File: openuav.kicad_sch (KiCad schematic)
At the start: 69 parts, among them J1 Conn_01x01, J10 Conn_01x01, J11 Conn_01x01, J12 Conn_01x01, J13 Conn_01x01, J14 Conn_01x01, J15 Conn_01x01, J16 Conn_01x01, J17 Conn_01x01, J18 Conn_01x01, J19 Conn_01x01, J2 Conn_01x01, J20 Conn_01x01, J21 Conn_01x01, J22 Conn_01x01, J23 Conn_01x01, J24 Conn_01x01, J25 Conn_01x01, J26 Conn_01x01, J27 Conn_01x01, J28 Conn_01x01, J29 Conn_01x01, J3 Conn_01x01, J30 Conn_01x01, J31 Conn_01x01, J4 Conn_01x01, J5 Conn_01x01, J6 Conn_01x01, J7 Conn_01x01, J8 Conn_01x01, J9 Conn_01x01, J99 USB_C_Receptacle_USB2.0, SW1 SW_Push, U1 STM32G474CETx, U2 BMI270, U3 BMP280, U5 TPS54202DDC, U6 W25N01GVZEIG, U7 XC6206P332MR

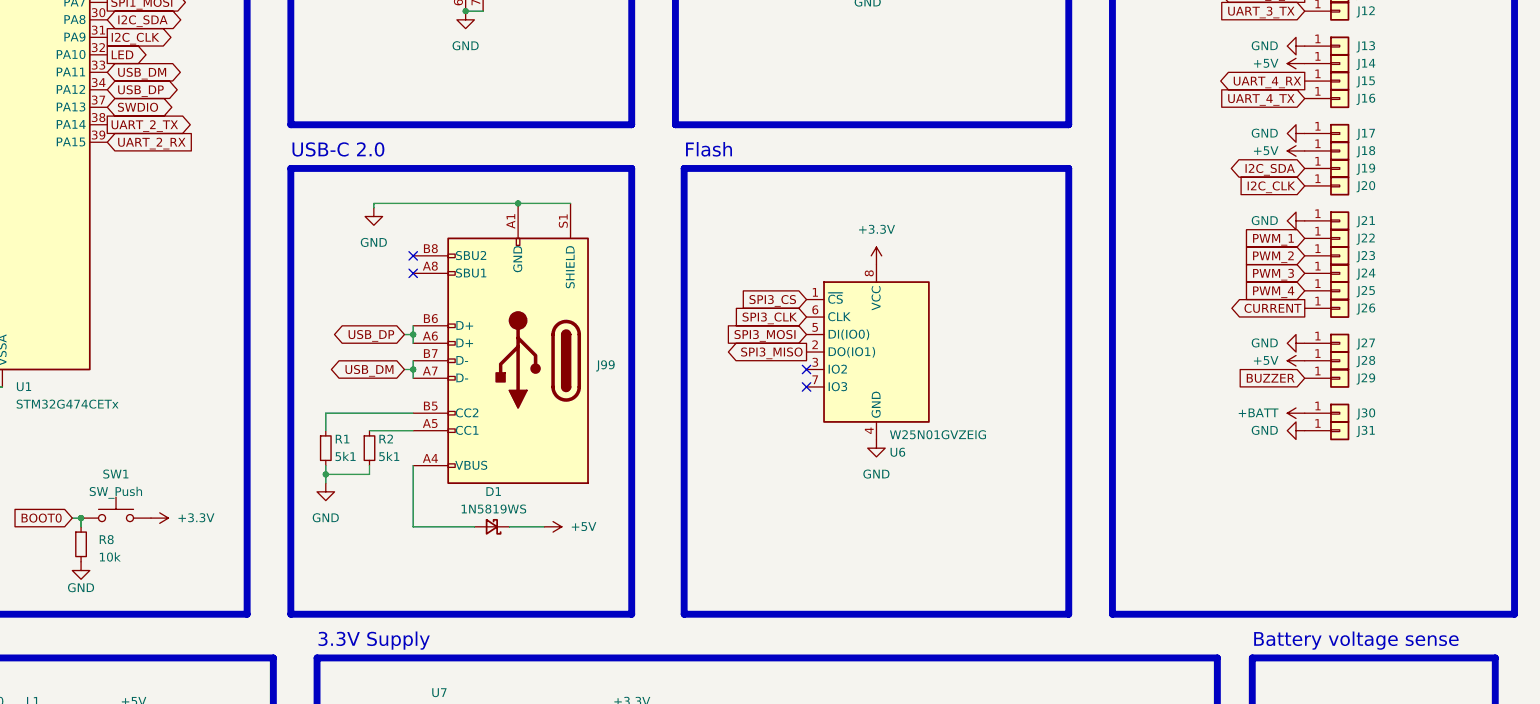
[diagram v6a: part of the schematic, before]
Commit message: continues work on G474 layout TODO: the pin space is 2.5mm not 2.54mm
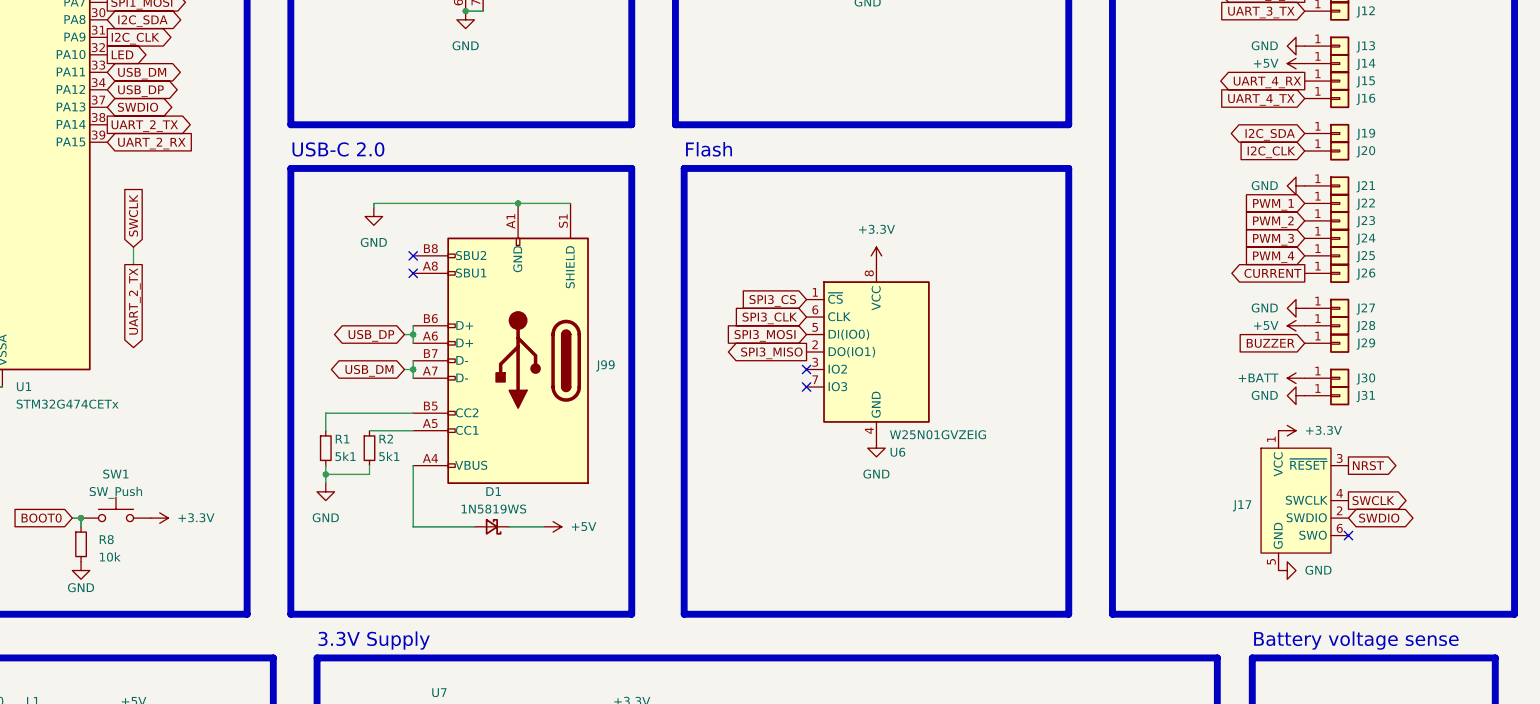
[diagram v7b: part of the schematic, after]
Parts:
- removed J17, J18: Conn_01x01, Connector_Custom_Pads:TP-2.54, symbol Connector_Generic:Conn_01x01
- added J17: Conn_ARM_SWD_TagConnect_TC2030-NL, Connector:Tag-Connect_TC2030-IDC-NL_2x03_P1.27mm_Vertical, symbol Connector:Conn_ARM_SWD_TagConnect_TC2030-NL
- SW1: footprint (none) -> Connector_Custom_Pads:TS-1187A-B-A-B; LCSC (none) -> C318884
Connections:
- net +3V3: now also J17.1 (VCC)
- net GND: now also J17.5 (GND)
- net NRST: now also J17.3 (~{RESET})
- net SWDIO: now also J17.2 (SWDIO)
- net UART_2_TX renamed SWCLK
- net SWCLK: now also J17.4 (SWCLK)
- no-connect marks 9 -> 10
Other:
- moved on the sheet: J19, J20, J21, J22, J23, J24, J25, J26, J27, J28, J29, J30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

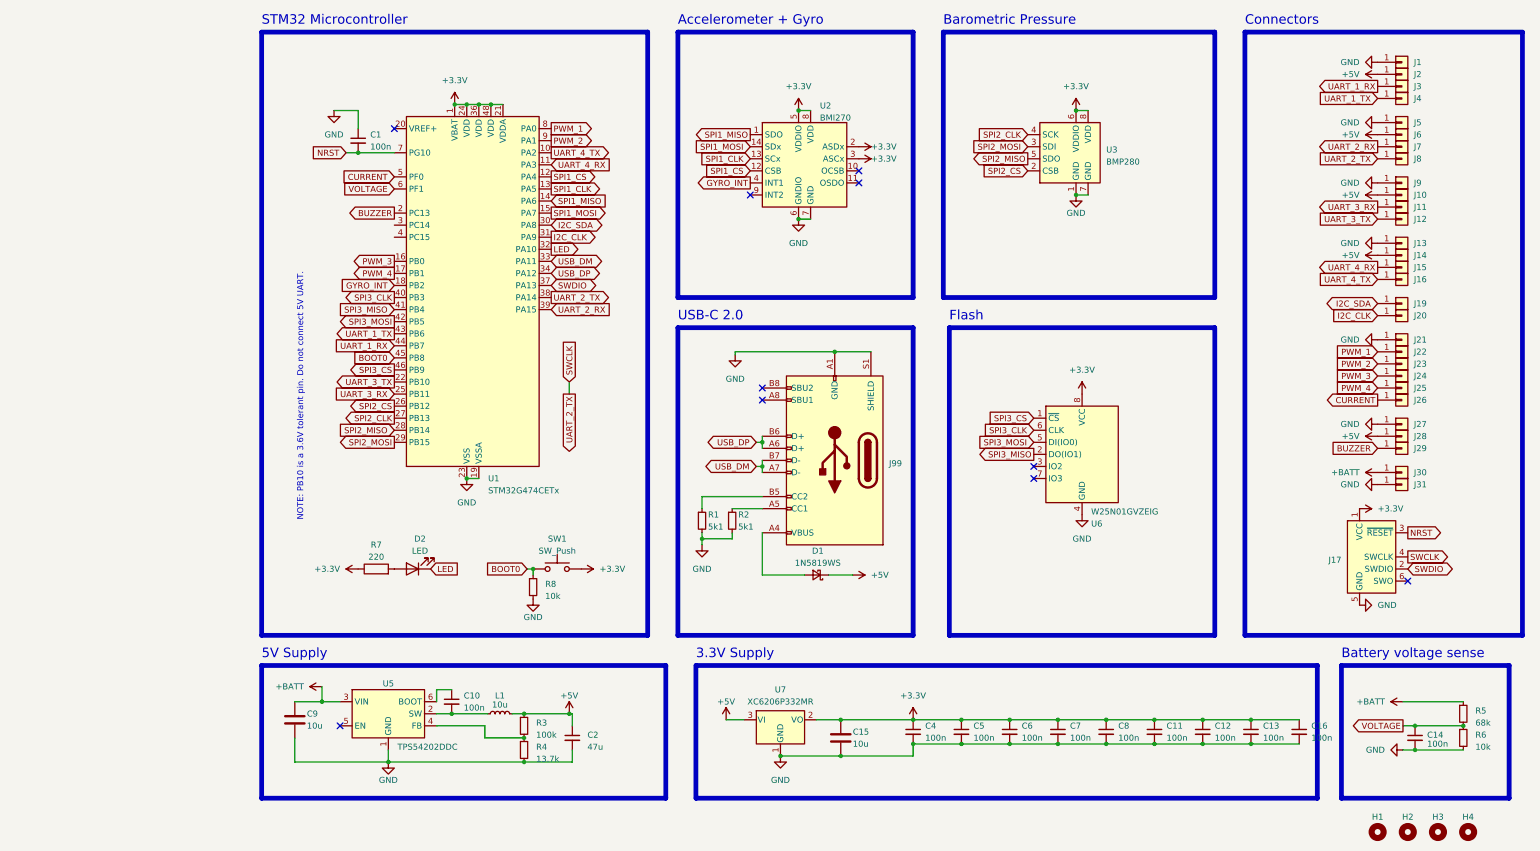
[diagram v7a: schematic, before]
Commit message: finish G474 layout, add buzzer buffer, add pullups, fix pin spacing
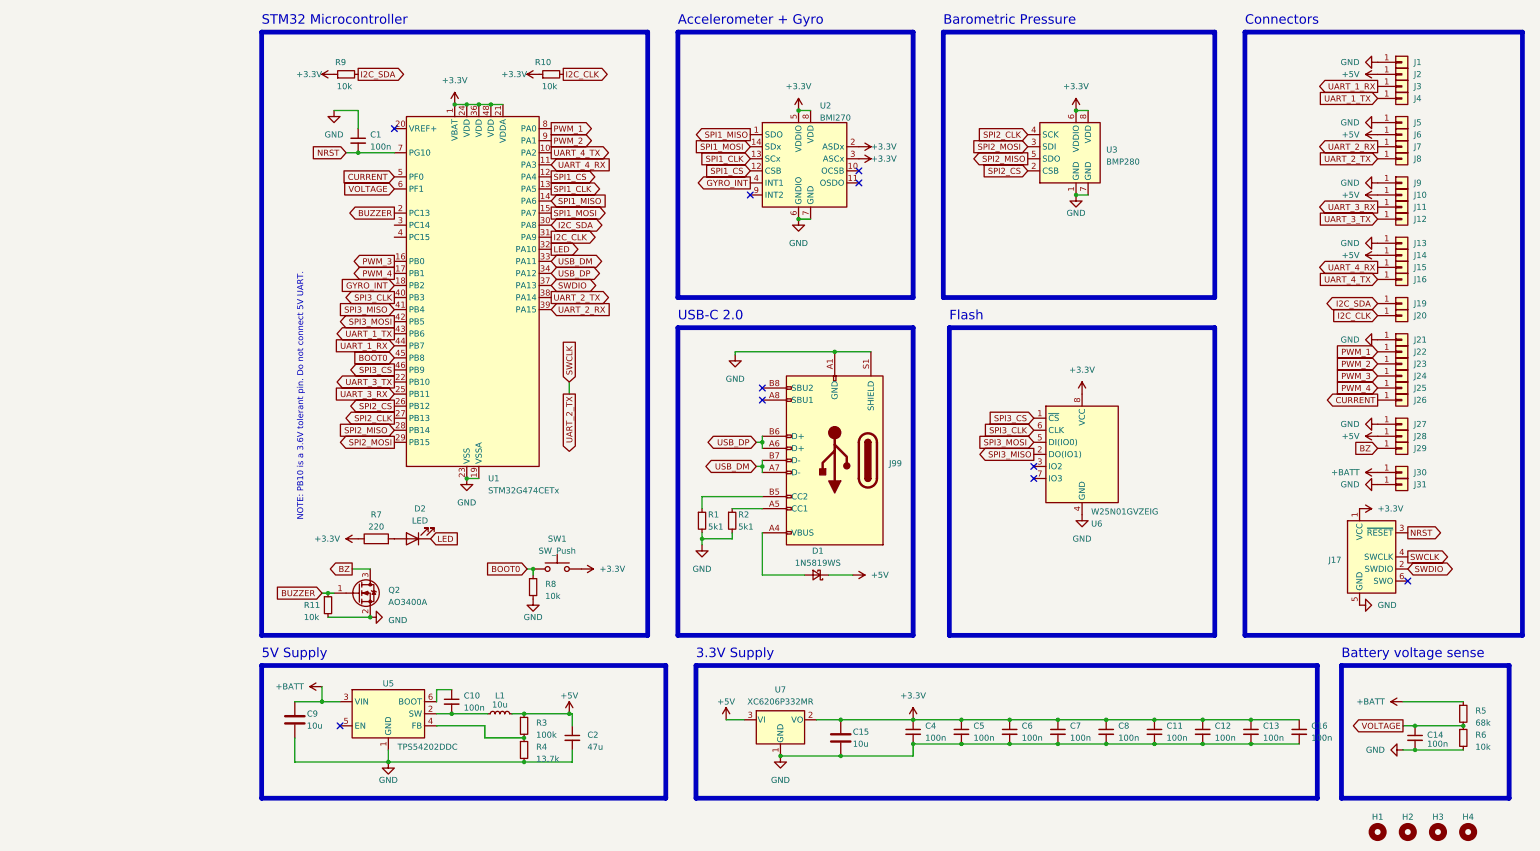
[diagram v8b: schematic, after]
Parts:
- added Q2: AO3400A, Package_TO_SOT_SMD:SOT-23, symbol Transistor_FET:AO3400A
- added R10, R11, R9: 10k, Resistor_SMD:R_0402_1005Metric, symbol Device:R_Small
- U1: LCSC (none) -> C730125
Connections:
- net +3V3: now also R10.1, R9.1
- net BUZZER: now also Q2.1 (G), R11.1; no longer J29.1 (Pin_1)
- net GND: now also Q2.2 (S), R11.2
- net I2C_CLK: now also R10.2
- net I2C_SDA: now also R9.2
- new net BZ: J29.1 (Pin_1), Q2.3 (D)
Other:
- moved on the sheet: D2, R7
